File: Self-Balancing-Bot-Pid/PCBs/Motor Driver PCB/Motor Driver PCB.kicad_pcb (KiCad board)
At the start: 2 copper layers, 42 x 42 mm, 27 parts, among them IC1 AS5600-ASOT, J1 Conn_01x08_Pin, U1 A4988SETTR-T

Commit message: Made sure PWR flags are all pointed up and GND flags are pointed down
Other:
- board text added: "StepDrive v1.0 July 2026"
- board text removed: "Maximelio Finch StepDrive v1.0 July 2026"

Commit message: Started rerouting and placing components and terminals in more elegant places. Expanded the copper pour and brought the as5600 IC to the front side.
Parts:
- C10: value 100uF -> 100uF/50V; footprint Capacitor_SMD:C_0603_1608Metric -> Capacitor_SMD:CP_Elec_8x10.5
- C9, IC1: moved to F.Cu
- R4, R5: value 0.05 -> 0.05Ω; footprint Resistor_SMD:R_0603_1608Metric -> Resistor_SMD:R_2512_6332Metric
- R6: value 20k -> 33k
- moved R7 13.7 mm to (174.8, 89.5), turned to 90 degrees
- moved C9 11.5 mm to (178.8, 101.2), turned to 0 degrees
- moved C6 10.1 mm to (179.8, 85.2)
- moved C1 9.43 mm to (179.8, 88.8)
- moved R3 9.33 mm to (174.8, 95.2)
- moved U1 8.96 mm to (179.5, 94.2)
- moved C10 8.69 mm to (189.9, 89.2), turned to 180 degrees
- moved C7 8.61 mm to (174.8, 92.2)
- moved R4 8.14 mm to (192.0, 109.0), turned to -90 degrees
- moved RV1 7.62 mm to (189.5, 118.0)
- moved R1 6.97 mm to (178.8, 99.8)
- moved R5 6.95 mm to (186.2, 109.5), turned to -90 degrees
- moved C4 4.93 mm to (179.5, 110.2)
- moved R6 3.47 mm to (179.5, 108.8)
- moved C8 2.88 mm to (179.5, 106.8)
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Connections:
- net /DIR renamed /DIR_B
- net Net-(J1-Pin_2) renamed /MS1
- net Net-(J1-Pin_3) renamed /MS2
- net Net-(J1-Pin_4) renamed /MS3
- net Net-(MC1-Pin_3) renamed /OUT2A
- net Net-(U1-REF) renamed /REF
- net Net-(U1-~{RESET}) renamed /SLEEP
- J1 pad 1: Net-(J1-Pin_1) -> /ENABLE
- J1 pad 5: Net-(J1-Pin_5) -> /STEP
- J1 pad 6: Net-(J1-Pin_6) -> /DIR_A
- MC1 pad 1: Net-(MC1-Pin_1) -> /OUT1B
- MC1 pad 2: Net-(MC1-Pin_2) -> /OUT1A
- MC1 pad 4: Net-(MC1-Pin_4) -> /OUT2B
- R7 pad 1: Net-(J1-Pin_6) -> /ENABLE
- U1 pad 1: Net-(MC1-Pin_1) -> /OUT2B
- U1 pad 16: Net-(J1-Pin_1) -> /STEP
- U1 pad 19: Net-(J1-Pin_5) -> /DIR_A
- U1 pad 2: Net-(J1-Pin_6) -> /ENABLE
- U1 pad 21: Net-(MC1-Pin_2) -> /OUT1B
- U1 pad 24: Net-(MC1-Pin_4) -> /OUT1A
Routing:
- net Net-(J1-Pin_1): track 29.9 -> 0.00 mm, vias 4 -> 0
- net /OUT1B: track 0.00 -> 23.8 mm
- net /OUT2B: track 0.00 -> 23.8 mm, vias 0 -> 2
- net /OUT1A: track 0.00 -> 22.9 mm
- net Net-(MC1-Pin_1): track 22.4 -> 0.00 mm, vias 1 -> 0
- net Net-(J1-Pin_6): track 21.3 -> 0.00 mm, vias 2 -> 0
- net Net-(J1-Pin_5): track 21.2 -> 0.00 mm, vias 4 -> 0
- net /REF: track 5.85 -> 25.6 mm, vias 0 -> 2
- net VDD: track 49.9 -> 31.1 mm, vias 0 -> 2
- net Net-(U1-SENSE2): track 3.35 -> 21.4 mm, vias 0 -> 2
- net /DIR_B: track 14.8 -> 31.8 mm, vias 0 -> 2
- net Net-(U1-SENSE1): track 2.98 -> 19.6 mm, vias 0 -> 2
- net Net-(MC1-Pin_2): track 15.3 -> 0.00 mm
- net Net-(MC1-Pin_4): track 15.2 -> 0.00 mm, vias 2 -> 0
- net /ENABLE: track 0.00 -> 15.1 mm, vias 0 -> 2
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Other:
- board text removed: "StepDrive v1.0 July 2026"

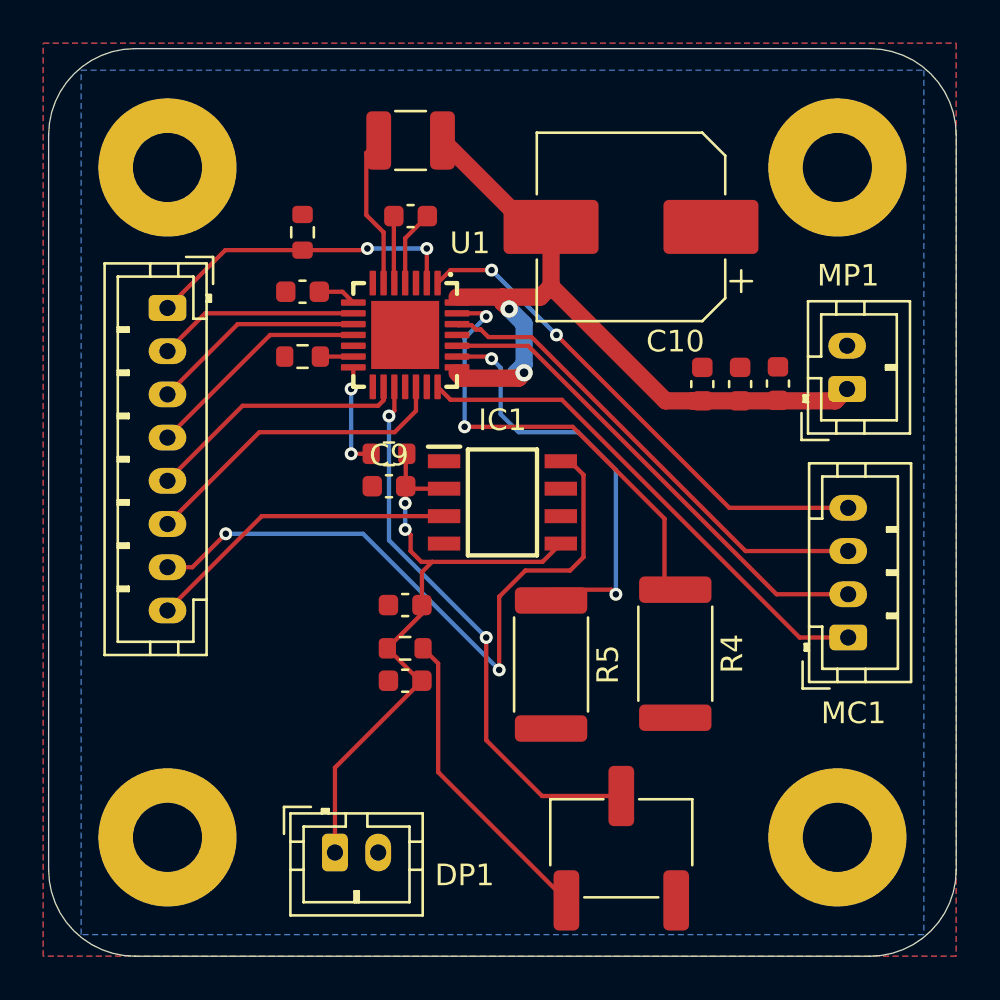
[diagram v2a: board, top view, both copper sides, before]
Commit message: Finished rerouting traces and vias, created new netclass for motor outputs.
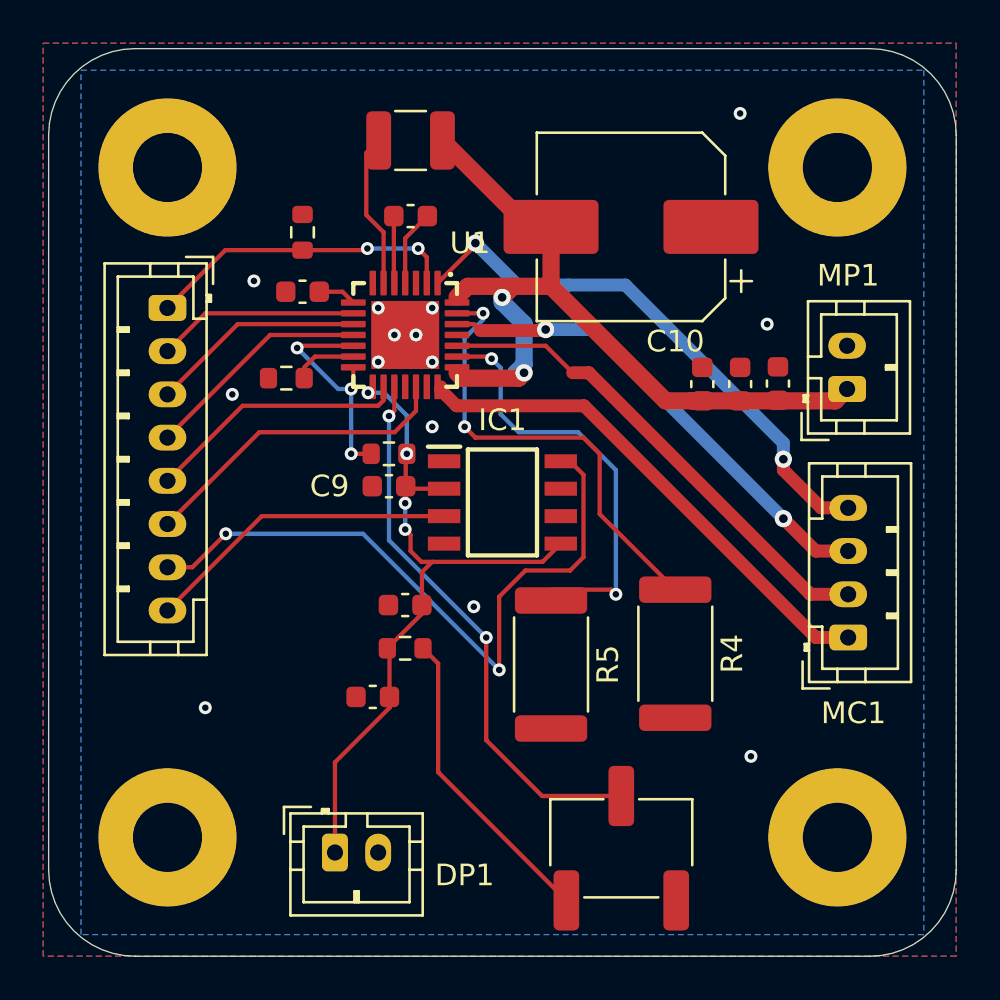
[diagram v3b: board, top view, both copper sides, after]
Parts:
- moved C4 1.68 mm to (178.0, 111.0)
- moved R3 1.25 mm to (174.0, 96.2)
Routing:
- net /SLEEP: track 4.97 -> 10.9 mm, vias 2 -> 3
- net VDD: track 31.1 -> 34.3 mm, vias 2 -> 4
- net /OUT2B: track 23.8 -> 25.6 mm
- net Net-(U1-ROSC): track 1.53 -> 2.48 mm
- net +12V: track 38.3 -> 39.1 mm
- net /OUT2A: track 22.4 -> 22.6 mm, vias 0 -> 2
- net GND: vias 0 -> 14

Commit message: Increased size of sense traces as they were too skinny
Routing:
- net Net-(U1-SENSE2): track 21.3 -> 19.4 mm
- net Net-(U1-SENSE1): track 19.6 -> 18.5 mm
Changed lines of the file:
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@@
 	)
 	(segment
-		(start 187.779204 97.529204)
-		(end 181.879204 97.529204)
-		(width 0.6)
-		(layer "F.Cu")
-		(net 17)
-	)
-	(segment
-		(start 200 108.25)
-		(end 198.5 108.25)
+		(start 199.5 108.25)
+		(end 188.25 97)
 		(width 0.6)
 		(layer "F.Cu")
@@
 	)
 	(segment
-		(start 198.5 108.25)
-		(end 187.779204 97.529204)
-		(width 0.6)
-		(layer "F.Cu")
-		(net 17)
-	)
-	(segment
-		(start 181.879204 97.529204)
+		(start 200 108.25)
+		(end 199.5 108.25)
+		(width 0.6)
+		(layer "F.Cu")
+		(net 17)
+	)
+	(segment
+		(start 185.274206 97)
+		(end 185.123206 97.151)
+		(width 0.6)
+		(layer "F.Cu")
+		(net 17)
+	)
+	(segment
+		(start 188.25 97)
+		(end 185.274206 97)
+		(width 0.6)
+		(layer "F.Cu")
+		(net 17)
+	)
+	(segment
+		(start 181.35 97)
 		(end 181.151 96.801)
+		(width 0.6)
+		(layer "F.Cu")
+		(net 17)
+	)
+	(segment
+		(start 181.624794 97)
+		(end 181.35 97)
+		(width 0.6)
+		(layer "F.Cu")
+		(net 17)
+	)
+	(segment
+		(start 185.123206 97.151)
+		(end 181.775793 97.150999)
+		(width 0.6)
+		(layer "F.Cu")
+		(net 17)
+	)
+	(segment
+		(start 181.775793 97.150999)
+		(end 181.624794 97)
 		(width 0.6)
 		(layer "F.Cu")
@@
 	)
 	(segment
-		(start 186 94.75)
-		(end 187.25 96)
+		(start 188 95.25)
+		(end 187.5 94.75)
 		(width 0.2)
 		(layer "F.Cu")
@@
 	)
 	(segment
-		(start 188 96)
-		(end 187.25 96)
+		(start 199 106.25)
+		(end 200 106.25)
 		(width 0.6)
 		(layer "F.Cu")
@@
 	)
 	(segment
-		(start 198.25 106.25)
-		(end 188 96)
+		(start 188 95.25)
+		(end 199 106.25)
 		(width 0.6)
 		(layer "F.Cu")
@@
 	)
 	(segment
-		(start 181.9 94.75)
-		(end 186 94.75)
-		(width 0.2)
-		(layer "F.Cu")
-		(net 19)
-	)
-	(segment
-		(start 200 106.25)
-		(end 198.25 106.25)
-		(width 0.6)
+		(start 187.5 94.75)
+		(end 181.9 94.75)
+		(width 0.2)
 		(layer "F.Cu")
 		(net 19)
@@
 	)
 	(segment
-		(start 183.101 93.25)
-		(end 181.9 93.25)
-		(width 0.2)
-		(layer "F.Cu")
-		(net 22)
-	)
-	(segment
-		(start 187.75 99)
-		(end 188.5 99.75)
-		(width 0.2)
-		(layer "F.Cu")
-		(net 22)
-	)
-	(segment
-		(start 182.75 99)
-		(end 187.75 99)
-		(width 0.2)
-		(layer "F.Cu")
-		(net 22)
-	)
-	(segment
-		(start 188.5 102.5375)
+		(start 183.146961 93.146961)
+		(end 183.079598 93.146961)
+		(width 0.2)
+		(layer "F.Cu")
+		(net 22)
+	)
+	(segment
+		(start 192.25 104)
+		(end 192.25 105.7875)
+		(width 0.6)
+		(layer "F.Cu")
+		(net 22)
+	)
+	(segment
+		(start 183.25 93.25)
+		(end 183.146961 93.146961)
+		(width 0.2)
+		(layer "F.Cu")
+		(net 22)
+	)
+	(segment
+		(start 192.25 105.7875)
 		(end 192 106.0375)
-		(width 0.2)
-		(layer "F.Cu")
-		(net 22)
-	)
-	(segment
-		(start 182.25 98.5)
-		(end 182.75 99)
-		(width 0.2)
-		(layer "F.Cu")
-		(net 22)
-	)
-	(segment
-		(start 188.5 99.75)
-		(end 188.5 102.5375)
-		(width 0.2)
-		(layer "F.Cu")
-		(net 22)
-	)
-	(segment
-		(start 183.10504 93.24596)
-		(end 183.101 93.25)
-		(width 0.2)
-		(layer "F.Cu")
-		(net 22)
-	)
-	(via
-		(at 182.25 98.5)
-		(size 0.6)
-		(drill 0.3)
-		(layers "F.Cu" "B.Cu")
-		(net 22)
-	)
-	(via
-		(at 183.10504 93.24596)
-		(size 0.6)
-		(drill 0.3)
-		(layers "F.Cu" "B.Cu")
-		(net 22)
-	)
-	(segment
-		(start 182.25 94.399)
-		(end 182.25 98.5)
-		(width 0.2)
-		(layer "B.Cu")
-		(net 22)
-	)
-	(segment
-		(start 183.10504 93.54396)
-		(end 182.25 94.399)
-		(width 0.2)
-		(layer "B.Cu")
-		(net 22)
-	)
-	(segment
-		(start 183.10504 93.24596)
-		(end 183.10504 93.54396)
-		(width 0.2)
-		(layer "B.Cu")
-		(net 22)
-	)
-	(segment
-		(start 189.25 106.25)
-		(end 189.0375 106.0375)
+		(width 0.6)
+		(layer "F.Cu")
+		(net 22)
+	)
+	(segment
+		(start 181.9 93.25)
+		(end 183.25 93.25)
+		(width 0.2)
+		(layer "F.Cu")
+		(net 22)
+	)
+	(via
+		(at 192.25 104)
+		(size 0.8)
+		(drill 0.4)
+		(layers "F.Cu" "B.Cu")
+		(net 22)
+	)
+	(via
+		(at 183.079598 93.146961)
+		(size 0.8)
+		(drill 0.4)
+		(layers "F.Cu" "B.Cu")
+		(net 22)
+	)
+	(segment
+		(start 183.079598 96.579598)
+		(end 185.25 98.75)
+		(width 0.6)
+		(layer "B.Cu")
+		(net 22)
+	)
+	(segment
+		(start 183.079598 93.146961)
+		(end 183.079598 96.579598)
+		(width 0.6)
+		(layer "B.Cu")
+		(net 22)
+	)
+	(segment
+		(start 187 98.75)
+		(end 192.25 104)
+		(width 0.6)
+		(layer "B.Cu")
+		(net 22)
+	)
+	(segment
+		(start 185.25 98.75)
+		(end 187 98.75)
+		(width 0.6)
+		(layer "B.Cu")
+		(net 22)
+	)
+	(segment
+		(start 185.5 95.25)
+		(end 186.25 96)
 		(width 0.2)
 		(layer "F.Cu")
@@
 	(segment
 		(start 181.9 95.25)
-		(end 183.4 95.25)
-		(width 0.2)
-		(layer "F.Cu")
-		(net 23)
-	)
-	(segment
-		(start 183.4 95.25)
-		(end 183.5 95.35)
-		(width 0.2)
-		(layer "F.Cu")
-		(net 23)
-	)
-	(segment
-		(start 189.0375 106.0375)
-		(end 186.25 106.0375)
-		(width 0.2)
-		(layer "F.Cu")
-		(net 23)
-	)
-	(via
-		(at 189.25 106.25)
-		(size 0.6)
-		(drill 0.3)
-		(layers "F.Cu" "B.Cu")
-		(net 23)
-	)
-	(via
-		(at 183.5 95.35)
-		(size 0.6)
-		(drill 0.3)
-		(layers "F.Cu" "B.Cu")
-		(net 23)
-	)
-	(segment
-		(start 183.5 95.35)
-		(end 183.919102 95.769102)
-		(width 0.2)
-		(layer "B.Cu")
-		(net 23)
-	)
-	(segment
-		(start 183.919102 95.769102)
-		(end 183.919102 97.919102)
-		(width 0.2)
-		(layer "B.Cu")
-		(net 23)
-	)
-	(segment
-		(start 184.75 98.75)
-		(end 187.5 98.75)
-		(width 0.2)
-		(layer "B.Cu")
-		(net 23)
-	)
-	(segment
-		(start 189.25 100.5)
-		(end 189.25 106.25)
-		(width 0.2)
-		(layer "B.Cu")
-		(net 23)
-	)
-	(segment
-		(start 187.5 98.75)
-		(end 189.25 100.5)
-		(width 0.2)
-		(layer "B.Cu")
-		(net 23)
-	)
-	(segment
-		(start 183.919102 97.919102)
-		(end 184.75 98.75)
-		(width 0.2)
-		(layer "B.Cu")
-		(net 23)
+		(end 185.5 95.25)
+		(width 0.2)
+		(layer "F.Cu")
+		(net 23)
+	)
+	(segment
+		(start 189.261397 99.738603)
+		(end 189.261397 104.988603)
+		(width 0.6)
+		(layer "F.Cu")
+		(net 23)
+	)
+	(segment
+		(start 187.7125 106.5375)
+		(end 186.25 106.5375)
+		(width 0.6)
+		(layer "F.Cu")
+		(net 23)
+	)
+	(segment
+		(start 189.261397 104.988603)
+		(end 187.7125 106.5375)
+		(width 0.6)
+		(layer "F.Cu")
+		(net 23)
+	)
+	(via
+		(at 186.25 96)
+		(size 0.8)
+		(drill 0.4)
+		(layers "F.Cu" "B.Cu")
+		(net 23)
+	)
+	(via
+		(at 189.261397 99.738603)
+		(size 0.8)
+		(drill 0.4)
+		(layers "F.Cu" "B.Cu")
+		(net 23)
+	)
+	(segment
+		(start 186.25 96)
+		(end 186.25 96.727206)
+		(width 0.6)
+		(layer "B.Cu")
+		(net 23)
+	)
+	(segment
+		(start 186.25 96.727206)
+		(end 189.261397 99.738603)
+		(width 0.6)
+		(layer "B.Cu")
+		(net 23)
